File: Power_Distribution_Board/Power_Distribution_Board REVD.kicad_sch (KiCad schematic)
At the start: 36 parts, among them J1 Conn_01x02, J10 Conn_01x02, J11 Conn_01x02, J3 Conn_01x02, J4 Conn_01x02, J5 Conn_01x05, J6 Conn_01x02, J7 Conn_01x02, J8 Conn_01x02, J9 Conn_01x02, U1 bmr480-45-to-60vin-12vout-130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, U2 PKU3511SPI

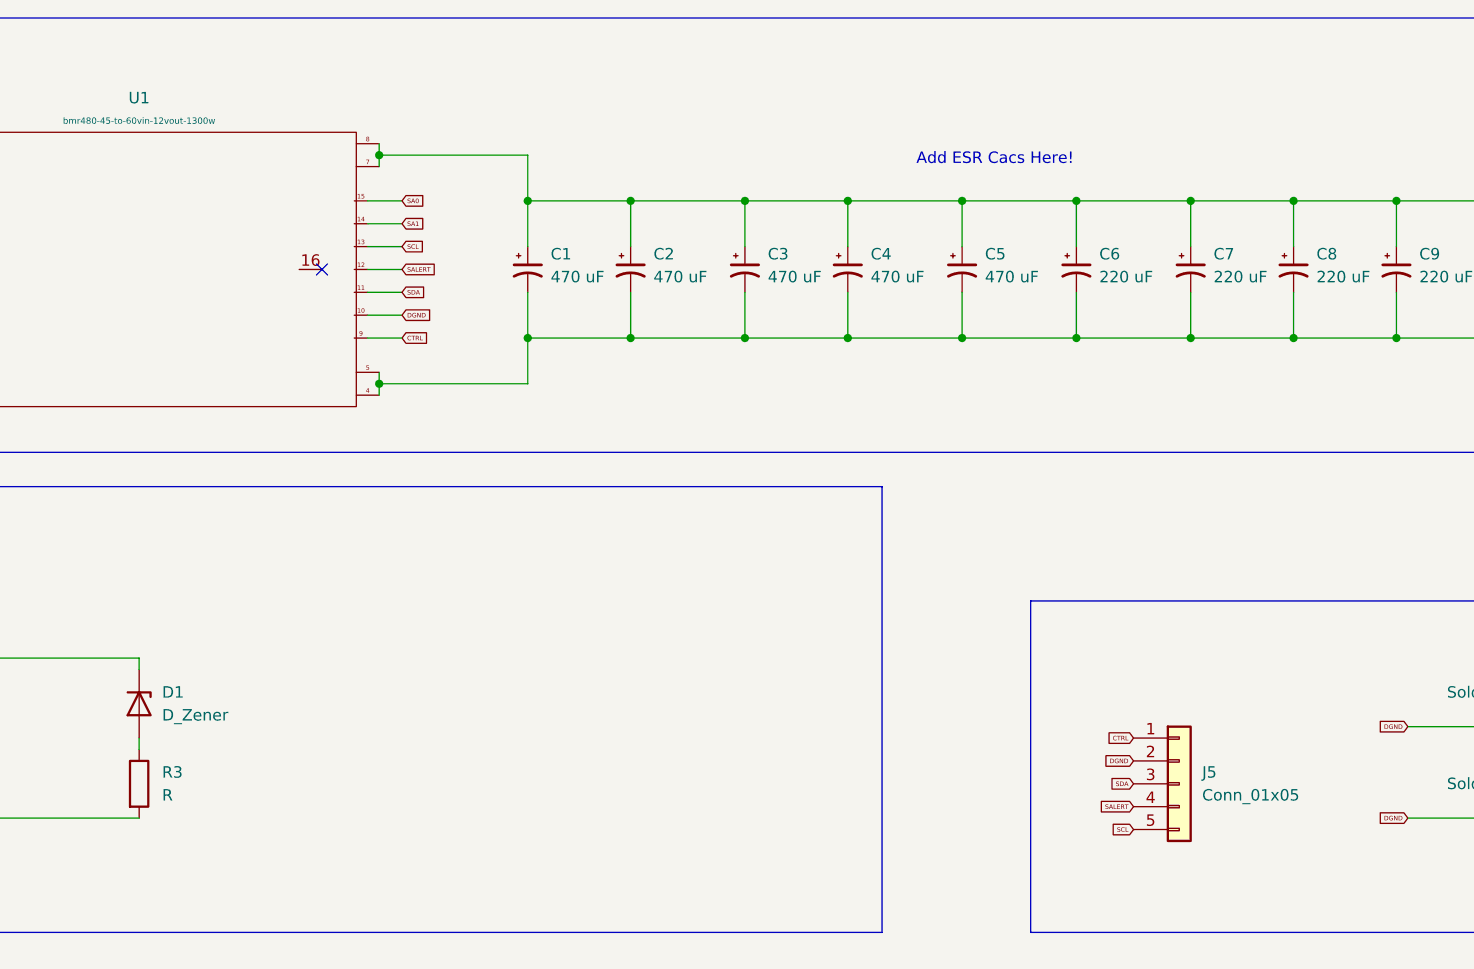
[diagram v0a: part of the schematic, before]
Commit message: Add schematic PDF and update KiCad schematic for Power Distribution Board
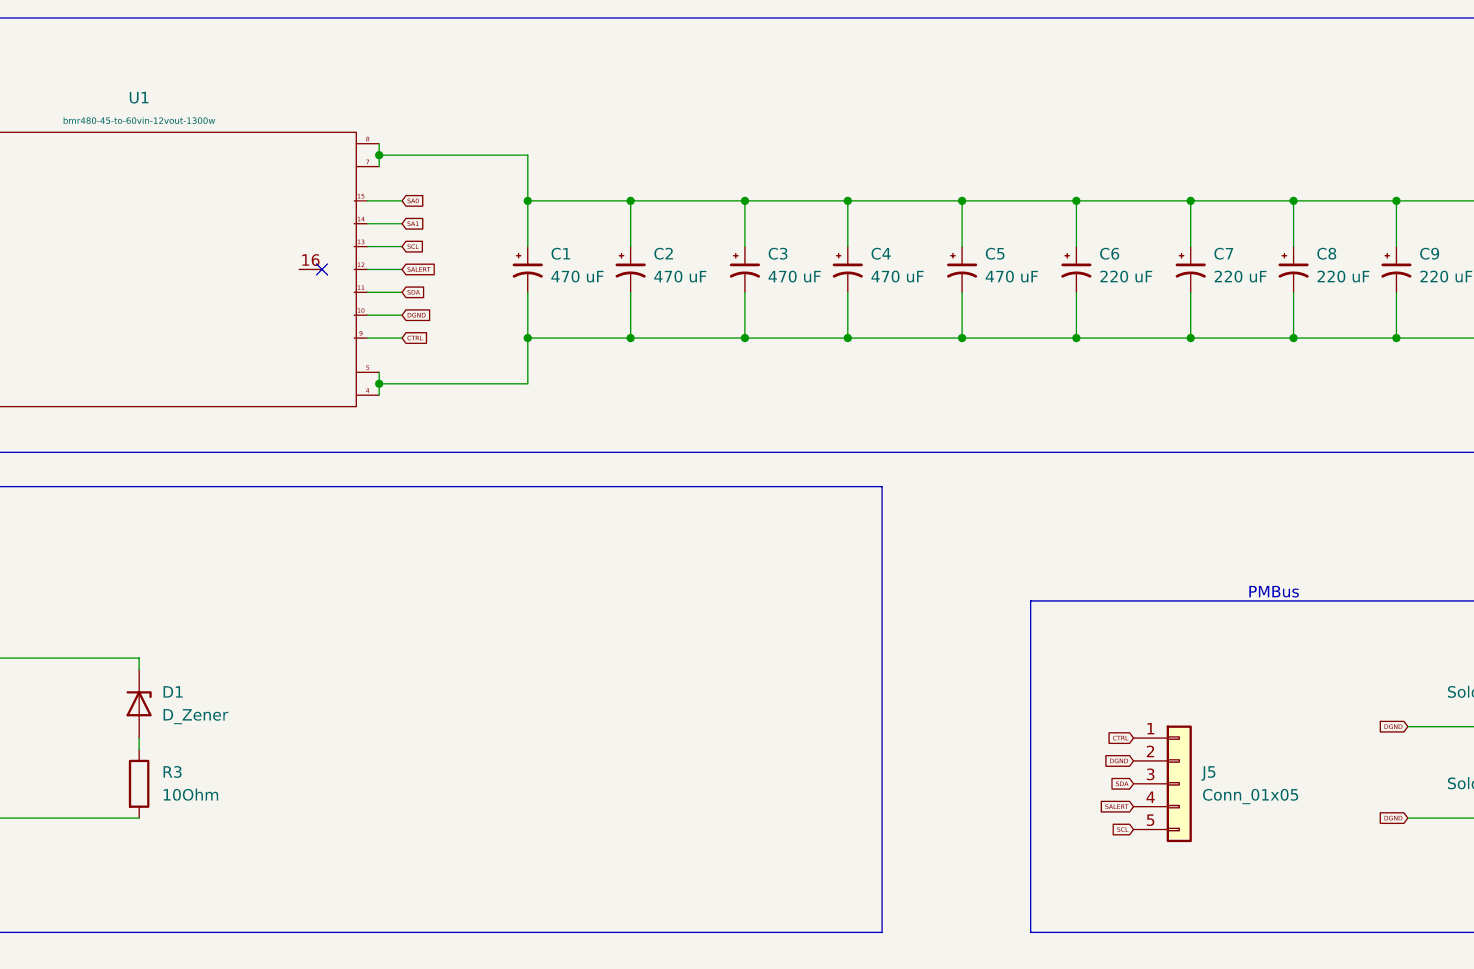
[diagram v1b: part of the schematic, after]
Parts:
- R3: value R -> 10Ohm
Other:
- note added: "PMBus"
- note removed: "Add ESR Cacs Here!"
- company: (none) -> Cabrillo Robotics, Seahawk II
- title: (none) -> Power Distrubtion Board
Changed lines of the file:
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@@
 (kicad_sch (version 20230121) (generator eeschema)
   (paper "A4")
+  (title_block
+    (title "Power Distrubtion Board")
+    (rev "V1.0")
+    (company "Cabrillo Robotics, Seahawk II")
+    (comment 1 "Clean up for release")
+  )
   (junction (at 177.8 52.07) (diameter 0) (color 0 0 0 0)
   )
@@
   (wire (pts (xy 251.46 95.25) (xy 261.62 95.25))
     (stroke (width 0) (type default))
-  )
-  (text "Add ESR Cacs Here!" (at 196.85 33.02 0)
-    (effects (font (size 1.27 1.27)) (justify left bottom))
   )
   (text "This can be used to increase or decrease the voatage\nNo pullup resitors will give the defult 5V\nSee how to spec resitors on p.19"
@@
   (text "without the need for control signals or a switch, the RC pin can\nbe wired directly to -In (p.21)"
     (at 41.91 193.04 0)
+    (effects (font (size 1.27 1.27)) (justify left bottom))
+  )
+  (text "PMBus" (at 233.68 81.28 0)
     (effects (font (size 1.27 1.27)) (justify left bottom))
   )
@@
       (effects (font (size 1.27 1.27)) (justify left))
     )
-    (property "Value" "R" (at 113.03 102.87 0)
-      (effects (font (size 1.27 1.27)) (justify left))
-    )
+    (property "Value" "10Ohm" (at 113.03 102.87 0)
+      (effects (font (size 1.27 1.27)) (justify left))
+    )
